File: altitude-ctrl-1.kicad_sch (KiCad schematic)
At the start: 70 parts, among them J1 Conn_01x02, J2 TC2030, J3 Conn_01x02, J4 Conn_01x02, J5 Conn_01x04_Pin, J6 Conn_01x02, SW1 SW_Push, SW2 SW_Push, SW3 SW_Push, U1 SN65HVD230, U2 LM73100, U3 HT753-1, U4 STM32F103C8Tx, U5 LM73100, Y1 8M

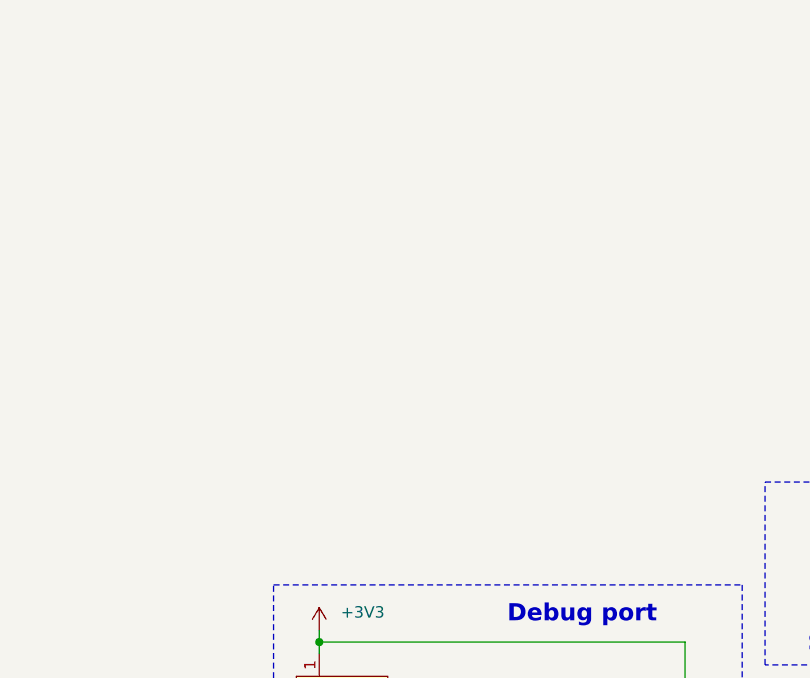
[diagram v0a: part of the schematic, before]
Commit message: schem: add MAX6675 Thermocouple ADC
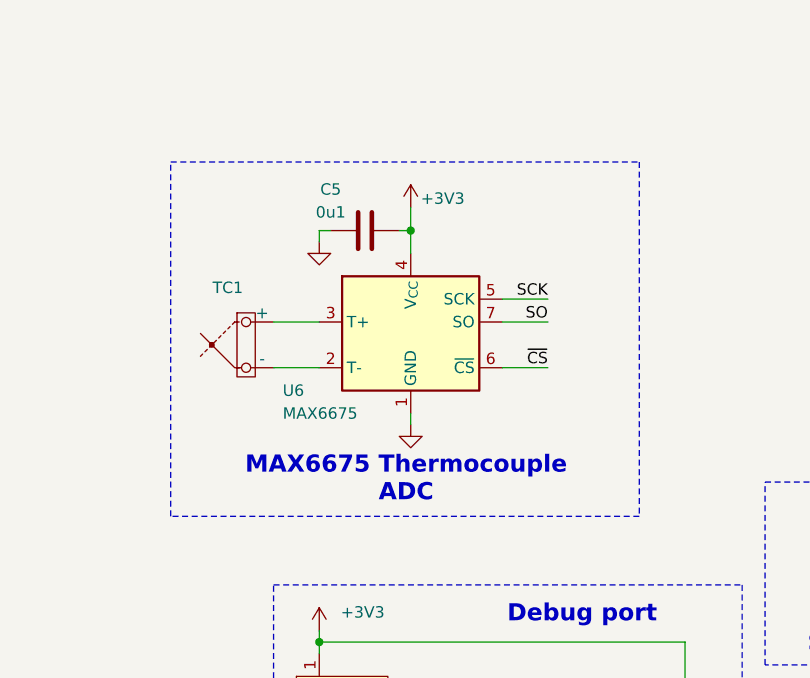
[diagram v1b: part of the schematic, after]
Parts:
- added C5: 0u1, Capacitor_SMD:C_0402_1005Metric, symbol Device:C
- added TC1: Thermocouple_Block, symbol Device:Thermocouple_Block
- added U6: MAX6675, Package_SO:SOIC-8_3.9x4.9mm_P1.27mm, symbol Sensor_Temperature:MAX31855KASA
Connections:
- net +3V3: now also C5.1, U6.4 (V_{CC})
- net GND: now also C5.2, U6.1 (GND)
- new net: TC1.1 (+), U6.3 (T+)
- new net: TC1.2 (-), U6.2 (T-)
- new net SCK: U6.5 (SCK)
- new net SO: U6.7 (SO)
- new net ~{CS}: U6.6 (~{CS})
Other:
- note added: "MAX6675 Thermocouple ADC"

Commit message: schem: add Current pressure sensor
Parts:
- added J7: Conn_01x02, symbol Connector_Generic:Conn_01x02
- added R14: 100, Resistor_SMD:R_0402_1005Metric, symbol Device:R
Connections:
- net +12V: now also J7.2 (Pin_2)
- net GND: now also R14.1
- new net PRES_SENSE: J7.1 (Pin_1), R14.2
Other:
- note added: "Current pressure sensor"

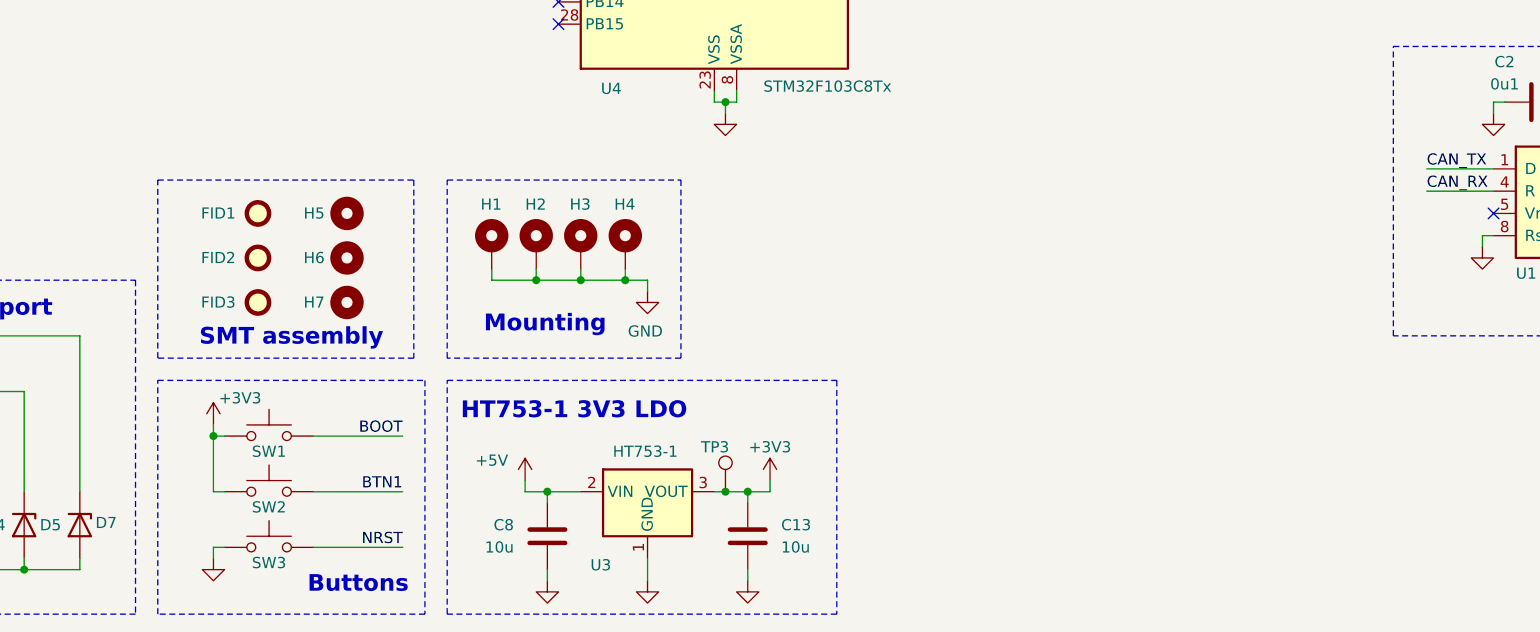
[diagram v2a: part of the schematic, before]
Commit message: schem: add BAU symbol
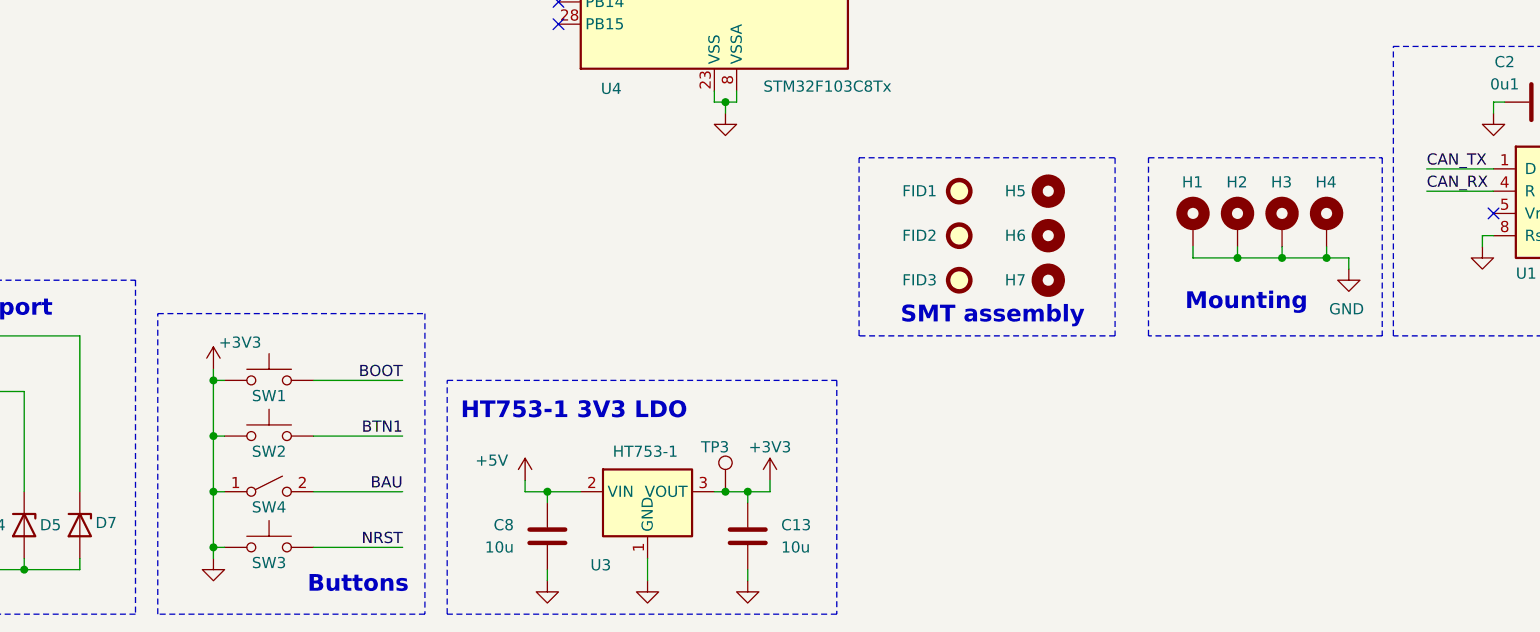
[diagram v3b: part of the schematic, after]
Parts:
- added SW4: SW_SPST, symbol Switch:SW_SPST
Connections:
- net GND is gone; now on net +3V3: C10.2, C11.2, C12.2, C13.2, C14.2, C15.2, C16.2, C17.2, C18.1, C19.1, C2.2, C20.1, C21.1, C22.1, C23.1, C3.1, C4.1, C5.2, C6.2, C7.2, C8.2, C9.2, D10.2 (A), D11.2 (A), D2.2 (A), D3.2 (A), D4.2 (A), D5.2 (A), D6.1 (K), D7.2 (A), D8.1 (K), D9.1 (K), H1.1, H2.1, H3.1, H4.1, J1.1 (Pin_1), J2.5 (GND), J5.3 (Pin_3), J6.1 (Pin_1), R10.2, R11.2, R14.1, R6.1, SW3.1, U1.2 (GND), U1.8 (Rs), U2.2 (OVCSEL), U2.8 (GND), U2.9 (ILM), U3.1 (GND), U4.20 (PB2), U4.23 (VSS), U4.35 (VSS), U4.47 (VSS), U4.8 (VSSA), U5.2 (OVCSEL), U5.8 (GND), U5.9 (ILM), U6.1 (GND)
- net +3V3: now also SW4.1 (A)
- new net BAU: SW4.2 (B)
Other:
- moved on the sheet: FID1, FID2, FID3, H1, H2, H3, H4, H5, H6, H7

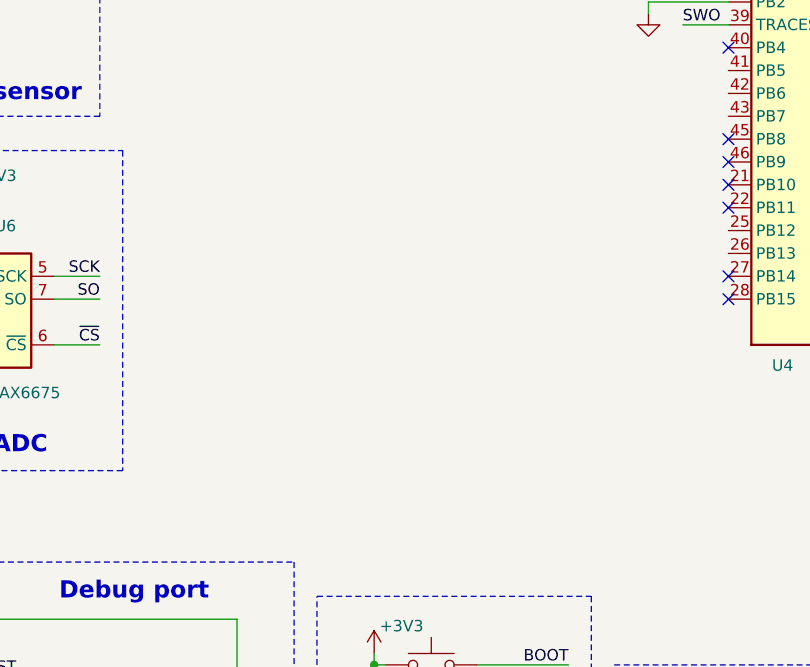
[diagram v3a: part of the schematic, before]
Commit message: schem: add relay driving circuit
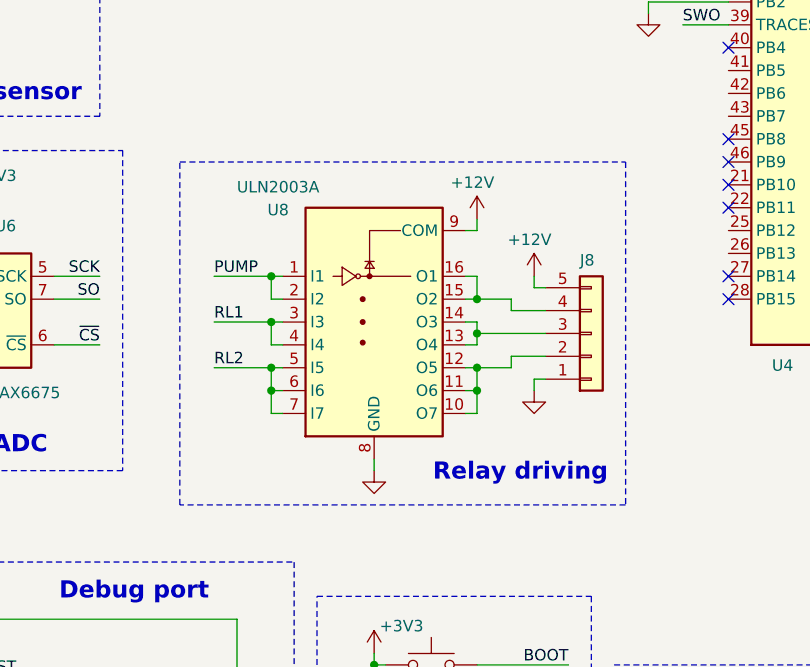
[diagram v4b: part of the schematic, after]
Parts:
- added J8: Conn_01x05, symbol Connector_Generic:Conn_01x05
- added U8: ULN2003A, Package_SO:SOIC-16_3.9x9.9mm_P1.27mm, symbol Transistor_Array:ULN2003A
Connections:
- net +12V: now also J8.5 (Pin_5), U8.9 (COM)
- net +3V3: now also J8.1 (Pin_1), U8.8 (GND)
- new net: J8.2 (Pin_2), U8.10 (O7), U8.11 (O6), U8.12 (O5)
- new net: J8.3 (Pin_3), U8.13 (O4), U8.14 (O3)
- new net: J8.4 (Pin_4), U8.15 (O2), U8.16 (O1)
- new net PUMP: U8.1 (I1), U8.2 (I2)
- new net RL1: U8.3 (I3), U8.4 (I4)
- new net RL2: U8.5 (I5), U8.6 (I6), U8.7 (I7)
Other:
- note added: "Relay driving"

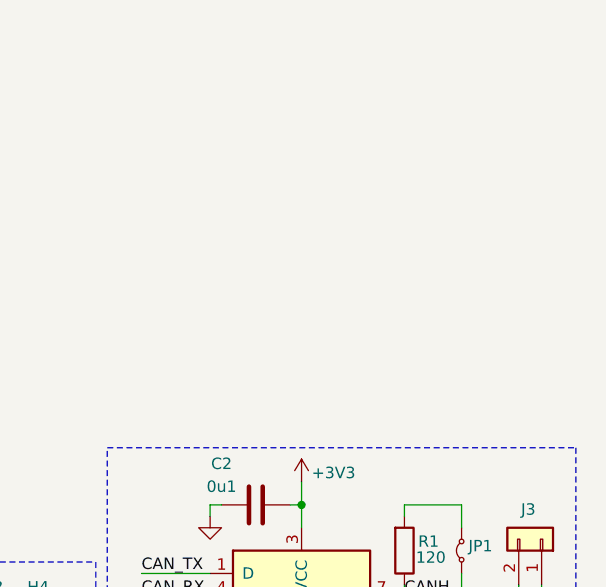
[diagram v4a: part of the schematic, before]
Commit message: schem: add MPRLS I2C connector
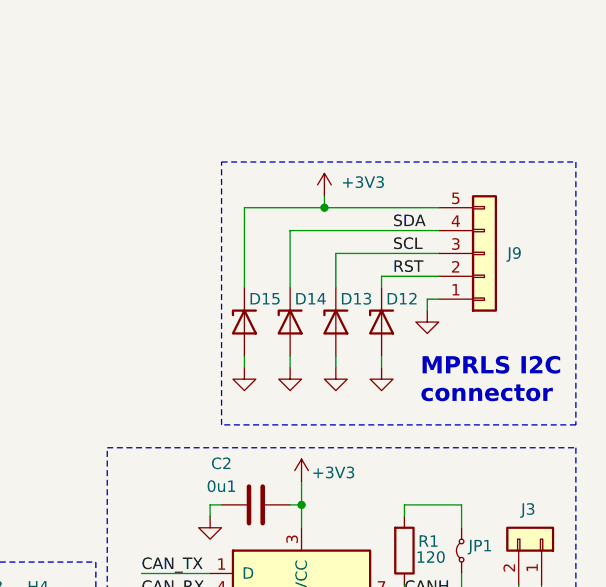
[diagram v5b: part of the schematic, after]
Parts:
- added D12, D13, D14, D15: H5VU10U, GLCS:Diode_DFN1006, symbol GLCS:H5VU10U
- added J9: Conn_01x05, symbol Connector_Generic:Conn_01x05
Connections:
- net +3V3: now also D12.2 (A), D13.2 (A), D14.2 (A), D15.1 (K), D15.2 (A), J9.1 (Pin_1), J9.5 (Pin_5)
- new net RST: D12.1 (K), J9.2 (Pin_2)
- new net SCL: D13.1 (K), J9.3 (Pin_3)
- new net SDA: D14.1 (K), J9.4 (Pin_4)
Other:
- note added: "MPRLS I2C connector"

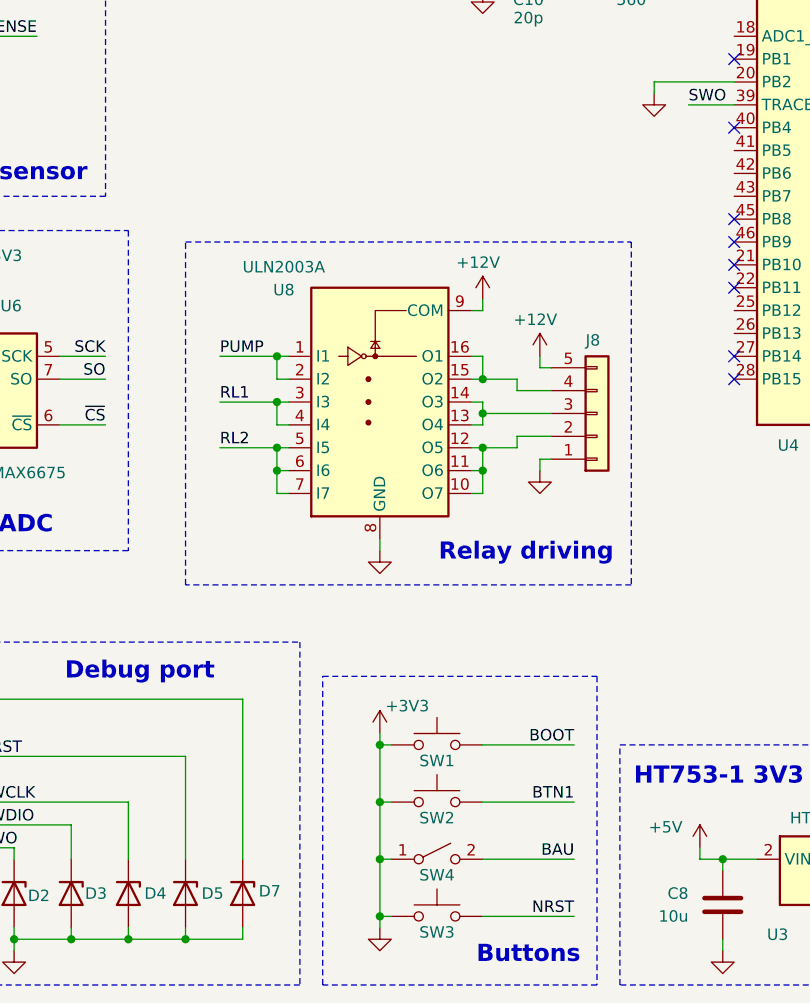
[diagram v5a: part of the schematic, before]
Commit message: schem: add LMS symbol
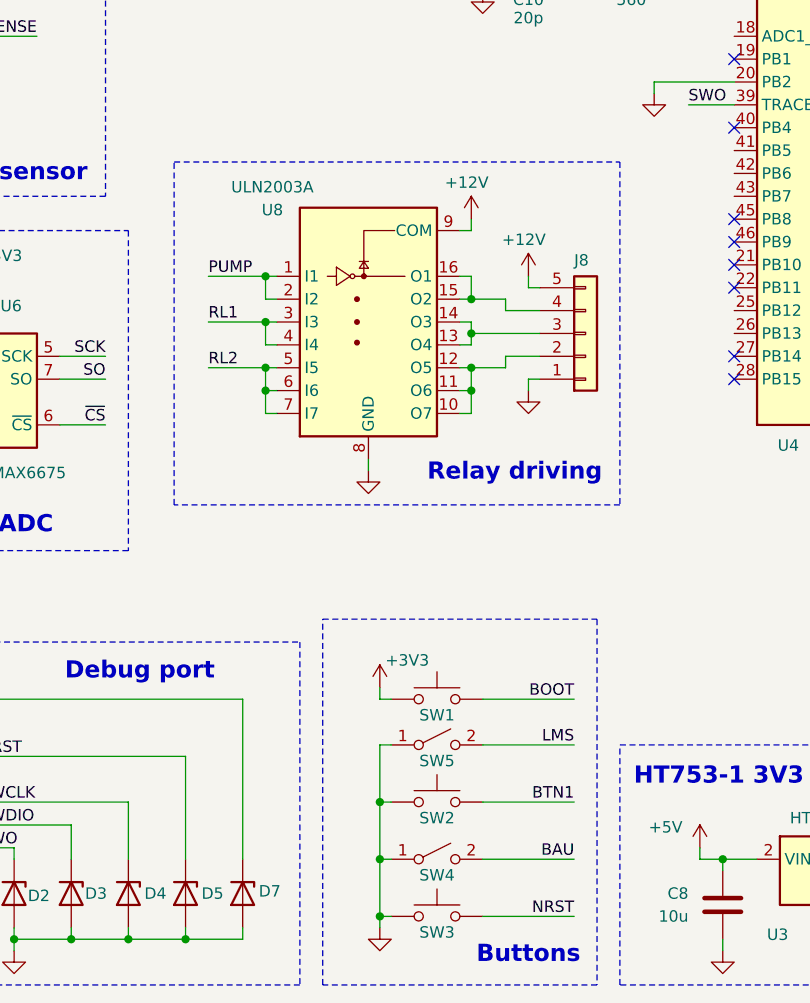
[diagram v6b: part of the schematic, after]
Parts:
- added SW5: SW_SPST, symbol Switch:SW_SPST
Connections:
- net +3V3: no longer C10.2, C11.2, C12.2, C13.2, C14.2, C15.2, C16.2, C17.2, C18.1, C19.1, C2.2, C20.1, C21.1, C22.1, C23.1, C3.1, C4.1, C5.2, C6.2, C7.2, C8.2, C9.2, D10.2 (A), D11.2 (A), D12.2 (A), D13.2 (A), D14.2 (A), D15.2 (A), D2.2 (A), D3.2 (A), D4.2 (A), D5.2 (A), D6.1 (K), D7.2 (A), D8.1 (K), D9.1 (K), H1.1, H2.1, H3.1, H4.1, J1.1 (Pin_1), J2.5 (GND), J5.3 (Pin_3), J6.1 (Pin_1), J8.1 (Pin_1), J9.1 (Pin_1), R10.2, R11.2, R14.1, R6.1, SW2.1, SW3.1, SW4.1 (A), U1.2 (GND), U1.8 (Rs), U2.2 (OVCSEL), U2.8 (GND), U2.9 (ILM), U3.1 (GND), U4.20 (PB2), U4.23 (VSS), U4.35 (VSS), U4.47 (VSS), U4.8 (VSSA), U5.2 (OVCSEL), U5.8 (GND), U5.9 (ILM), U6.1 (GND), U8.8 (GND)
- new net GND: C10.2, C11.2, C12.2, C13.2, C14.2, C15.2, C16.2, C17.2, C18.1, C19.1, C2.2, C20.1, C21.1, C22.1, C23.1, C3.1, C4.1, C5.2, C6.2, C7.2, C8.2, C9.2, D10.2 (A), D11.2 (A), D12.2 (A), D13.2 (A), D14.2 (A), D15.2 (A), D2.2 (A), D3.2 (A), D4.2 (A), D5.2 (A), D6.1 (K), D7.2 (A), D8.1 (K), D9.1 (K), H1.1, H2.1, H3.1, H4.1, J1.1 (Pin_1), J2.5 (GND), J5.3 (Pin_3), J6.1 (Pin_1), J8.1 (Pin_1), J9.1 (Pin_1), R10.2, R11.2, R14.1, R6.1, SW2.1, SW3.1, SW4.1 (A), SW5.1 (A), U1.2 (GND), U1.8 (Rs), U2.2 (OVCSEL), U2.8 (GND), U2.9 (ILM), U3.1 (GND), U4.20 (PB2), U4.23 (VSS), U4.35 (VSS), U4.47 (VSS), U4.8 (VSSA), U5.2 (OVCSEL), U5.8 (GND), U5.9 (ILM), U6.1 (GND), U8.8 (GND)
- new net LMS: SW5.2 (B)
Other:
- moved on the sheet: J8, SW1, U8

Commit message: schem: add stepper interface
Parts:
- added D16, D17, D18, D19: H5VU10U, GLCS:Diode_DFN1006, symbol GLCS:H5VU10U
- added J11: Conn_01x05, symbol Connector_Generic:Conn_01x05
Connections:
- net +5V: now also D16.1 (K), J11.5 (Pin_5)
- net GND: now also D16.2 (A), D17.2 (A), D18.2 (A), D19.2 (A), J11.1 (Pin_1)
- new net DIR: D18.1 (K), J11.3 (Pin_3)
- new net EN: D19.1 (K), J11.2 (Pin_2)
- new net STEP: D17.1 (K), J11.4 (Pin_4)
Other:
- note added: "Stepper Interface"
